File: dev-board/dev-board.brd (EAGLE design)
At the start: 49.2 x 64.8 mm, 44 parts, among them J1 12401832E402A, U1 STM32F103RET6, U2 AT24C64BN-10SU-2.7, U3 FT232RL, U4 MCP2551, U5 Value, X1 8MHz

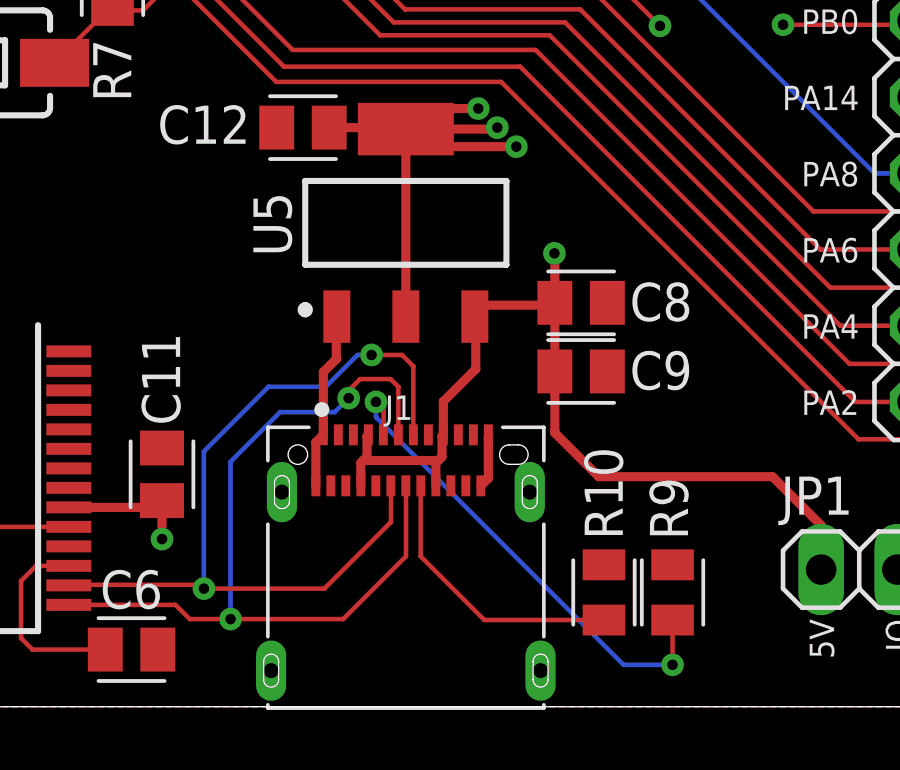
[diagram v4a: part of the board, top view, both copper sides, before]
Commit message: Move R9 to the opposite side of the connector
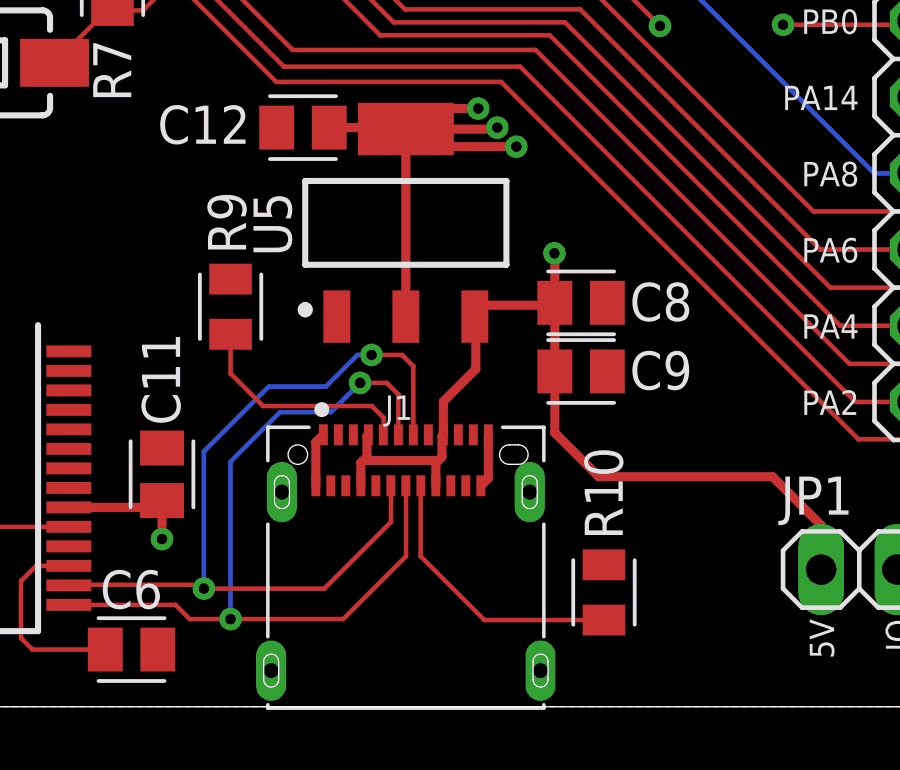
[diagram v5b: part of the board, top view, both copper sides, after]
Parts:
- moved R9 17.5 mm to (16.6, 13.3)
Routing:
- net N$13: track 16.5 -> 7.59 mm, vias 2 -> 0
- net GND: track 7.78 -> 3.66 mm
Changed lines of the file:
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@@
 <attribute name="TYPE" value="" x="55.88" y="69.85" size="1.778" layer="27" rot="R90" display="off"/>
 </element>
-<element name="R9" library="Resistor" library_urn="urn:adsk.eagle:library:16378527" package="RESC2012X65" package3d_urn="urn:adsk.eagle:package:16378559/2" value="5K1" x="31.369" y="3.81" smashed="yes" rot="R270">
-<attribute name="CATEGORY" value="Resistor" x="-21.971" y="-46.99" size="1.778" layer="27" rot="R270" display="off"/>
-<attribute name="MANUFACTURER" value="" x="-21.971" y="-46.99" size="1.778" layer="27" rot="R270" display="off"/>
-<attribute name="MPN" value="" x="-21.971" y="-46.99" size="1.778" layer="27" rot="R270" display="off"/>
-<attribute name="NAME" x="31.8851" y="6.604" size="1.27" layer="25" rot="R90" align="bottom-center"/>
-<attribute name="OPERATING_TEMP" value="" x="-21.971" y="-46.99" size="1.778" layer="27" rot="R270" display="off"/>
-<attribute name="PART_STATUS" value="" x="-21.971" y="-46.99" size="1.778" layer="27" rot="R270" display="off"/>
-<attribute name="RATING" value="" x="-21.971" y="-46.99" size="1.778" layer="27" rot="R270" display="off"/>
-<attribute name="ROHS_COMPLIANT" value="" x="-21.971" y="-46.99" size="1.778" layer="27" rot="R270" display="off"/>
-<attribute name="SERIES" value="" x="-21.971" y="-46.99" size="1.778" layer="27" rot="R270" display="off"/>
-<attribute name="SUB-CATEGORY" value="Fixed" x="-21.971" y="-46.99" size="1.778" layer="27" rot="R270" display="off"/>
-<attribute name="THERMALLOSS" value="" x="-21.971" y="-46.99" size="1.778" layer="27" rot="R270" display="off"/>
-<attribute name="TOLERANCE" value="" x="-21.971" y="-46.99" size="1.778" layer="27" rot="R270" display="off"/>
-<attribute name="TYPE" value="" x="-21.971" y="-46.99" size="1.778" layer="27" rot="R270" display="off"/>
+<element name="R9" library="Resistor" library_urn="urn:adsk.eagle:library:16378527" package="RESC2012X65" package3d_urn="urn:adsk.eagle:package:16378559/2" value="5K1" x="16.637" y="13.335" smashed="yes" rot="R270">
+<attribute name="CATEGORY" value="Resistor" x="-36.703" y="-37.465" size="1.778" layer="27" rot="R270" display="off"/>
+<attribute name="MANUFACTURER" value="" x="-36.703" y="-37.465" size="1.778" layer="27" rot="R270" display="off"/>
+<attribute name="MPN" value="" x="-36.703" y="-37.465" size="1.778" layer="27" rot="R270" display="off"/>
+<attribute name="NAME" x="17.1531" y="16.129" size="1.27" layer="25" rot="R90" align="bottom-center"/>
+<attribute name="OPERATING_TEMP" value="" x="-36.703" y="-37.465" size="1.778" layer="27" rot="R270" display="off"/>
+<attribute name="PART_STATUS" value="" x="-36.703" y="-37.465" size="1.778" layer="27" rot="R270" display="off"/>
+<attribute name="RATING" value="" x="-36.703" y="-37.465" size="1.778" layer="27" rot="R270" display="off"/>
+<attribute name="ROHS_COMPLIANT" value="" x="-36.703" y="-37.465" size="1.778" layer="27" rot="R270" display="off"/>
+<attribute name="SERIES" value="" x="-36.703" y="-37.465" size="1.778" layer="27" rot="R270" display="off"/>
+<attribute name="SUB-CATEGORY" value="Fixed" x="-36.703" y="-37.465" size="1.778" layer="27" rot="R270" display="off"/>
+<attribute name="THERMALLOSS" value="" x="-36.703" y="-37.465" size="1.778" layer="27" rot="R270" display="off"/>
+<attribute name="TOLERANCE" value="" x="-36.703" y="-37.465" size="1.778" layer="27" rot="R270" display="off"/>
+<attribute name="TYPE" value="" x="-36.703" y="-37.465" size="1.778" layer="27" rot="R270" display="off"/>
 </element>
 <element name="S1" library="SparkFun-Switches" library_urn="urn:adsk.eagle:library:535" package="TACTILE_SWITCH_SMD_6.0X3.5MM" package3d_urn="urn:adsk.eagle:package:40165/1" value="NRST" x="7.62" y="21.463" smashed="yes" rot="R180">
@@
 <wire x1="19.479" y1="7.364" x2="19.479" y2="8.814" width="0.3048" layer="1"/>
 <wire x1="19.479" y1="8.814" x2="19.729" y2="9.064" width="0.3048" layer="1"/>
-<wire x1="20.179" y1="11.607" x2="20.161" y2="11.589" width="0.3048" layer="1"/>
-<wire x1="20.161" y1="11.589" x2="19.729" y2="11.157" width="0.3048" layer="1"/>
-<wire x1="19.729" y1="11.157" x2="19.729" y2="9.064" width="0.3048" layer="1"/>
 <contactref element="C10" pad="2"/>
 <contactref element="C11" pad="2"/>
@@
 <contactref element="C8" pad="2"/>
 <contactref element="C9" pad="2"/>
-<wire x1="20.161" y1="11.589" x2="20.161" y2="12.986" width="0.3048" layer="1"/>
 <wire x1="20.161" y1="12.986" x2="20.179" y2="13.004" width="0.3048" layer="1"/>
 <wire x1="24.979" y1="7.364" x2="25.229" y2="7.614" width="0.3048" layer="1"/>
@@
 <contactref element="R9" pad="2"/>
 <contactref element="J1" pad="A5"/>
-<via x="21.4828" y="10.16" extent="1-16" drill="0.35"/>
-<wire x1="21.4828" y1="10.1414875" x2="21.4828" y2="10.16" width="0.1524" layer="1"/>
-<wire x1="21.737" y1="9.8872875" x2="21.737" y2="9.072" width="0.1524" layer="1"/>
 <wire x1="21.729" y1="9.064" x2="21.737" y2="9.072" width="0.1524" layer="1"/>
-<wire x1="21.737" y1="9.8872875" x2="21.4828" y2="10.1414875" width="0.1524" layer="1"/>
-<wire x1="29.7378" y1="1.397" x2="21.4828" y2="9.652" width="0.1524" layer="16"/>
-<wire x1="21.4828" y1="10.16" x2="21.4828" y2="9.652" width="0.1524" layer="16"/>
-<wire x1="29.7378" y1="1.397" x2="31.369" y2="1.397" width="0.1524" layer="16"/>
-<via x="31.369" y="1.397" extent="1-16" drill="0.35"/>
-<wire x1="31.369" y1="1.397" x2="31.369" y2="2.8905" width="0.1524" layer="1"/>
+<wire x1="21.3466875" y1="10.0236" x2="17.7214" y2="10.0236" width="0.1524" layer="1"/>
+<wire x1="16.637" y1="12.4155" x2="16.637" y2="11.108" width="0.1524" layer="1"/>
+<wire x1="17.7214" y1="10.0236" x2="16.637" y2="11.108" width="0.1524" layer="1"/>
+<wire x1="21.737" y1="9.6332875" x2="21.737" y2="9.072" width="0.1524" layer="1"/>
+<wire x1="21.737" y1="9.6332875" x2="21.3466875" y2="10.0236" width="0.1524" layer="1"/>
 </signal>
 <signal name="N$17">
@@
 <contactref element="J1" pad="A6"/>
 <contactref element="J1" pad="B6"/>
-<wire x1="22.229" y1="9.064" x2="22.229" y2="10.664" width="0.1524" layer="1"/>
-<wire x1="22.229" y1="10.664" x2="21.971" y2="10.922" width="0.1524" layer="1"/>
-<wire x1="21.971" y1="10.922" x2="20.955" y2="10.922" width="0.1524" layer="1"/>
-<wire x1="20.955" y1="10.922" x2="20.574" y2="10.541" width="0.1524" layer="1"/>
-<wire x1="20.574" y1="10.541" x2="20.574" y2="10.287" width="0.1524" layer="1"/>
-<via x="20.574" y="10.287" extent="1-16" drill="0.35"/>
+<wire x1="22.229" y1="9.064" x2="22.229" y2="10.41" width="0.1524" layer="1"/>
+<wire x1="22.229" y1="10.41" x2="21.844" y2="10.795" width="0.1524" layer="1"/>
+<wire x1="21.844" y1="10.795" x2="20.955" y2="10.795" width="0.1524" layer="1"/>
+<via x="20.955" y="10.795" extent="1-16" drill="0.35"/>
 <via x="16.637" y="2.921" extent="1-16" drill="0.35"/>
-<wire x1="20.574" y1="10.287" x2="20.1082" y2="9.8212" width="0.1524" layer="16"/>
-<wire x1="20.1082" y1="9.8212" x2="18.291975" y2="9.8212" width="0.1524" layer="16"/>
+<wire x1="20.955" y1="10.795" x2="19.9812" y2="9.8212" width="0.1524" layer="16"/>
+<wire x1="19.9812" y1="9.8212" x2="18.291975" y2="9.8212" width="0.1524" layer="16"/>
 <wire x1="18.291975" y1="9.8212" x2="16.637" y2="8.166225" width="0.1524" layer="16"/>
 <wire x1="16.637" y1="8.166225" x2="16.637" y2="2.921" width="0.1524" layer="16"/>

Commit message: Move 5V trace to the right a bit
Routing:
- net +5V: track 119.1 -> 118.5 mm
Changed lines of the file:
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@@
 <wire x1="17.1316" y1="6.5906" x2="16.129" y2="5.588" width="0.3048" layer="15"/>
 <wire x1="17.1316" y1="6.5906" x2="17.1316" y2="10.0385875" width="0.3048" layer="15"/>
-<wire x1="0.508" y1="4.826" x2="-1.27" y2="6.604" width="0.3048" layer="15"/>
-<wire x1="-1.27" y1="38.354" x2="7.493" y2="47.117" width="0.3048" layer="15"/>
-<wire x1="-1.27" y1="6.604" x2="-1.27" y2="38.354" width="0.3048" layer="15"/>
+<wire x1="0.508" y1="4.826" x2="-0.508" y2="5.842" width="0.3048" layer="15"/>
+<wire x1="-0.508" y1="39.116" x2="7.493" y2="47.117" width="0.3048" layer="15"/>
+<wire x1="-0.508" y1="5.842" x2="-0.508" y2="39.116" width="0.3048" layer="15"/>
 <contactref element="JP1" pad="1"/>
 <wire x1="27.4456" y1="9.1304" x2="28.908" y2="7.668" width="0.3048" layer="1"/>

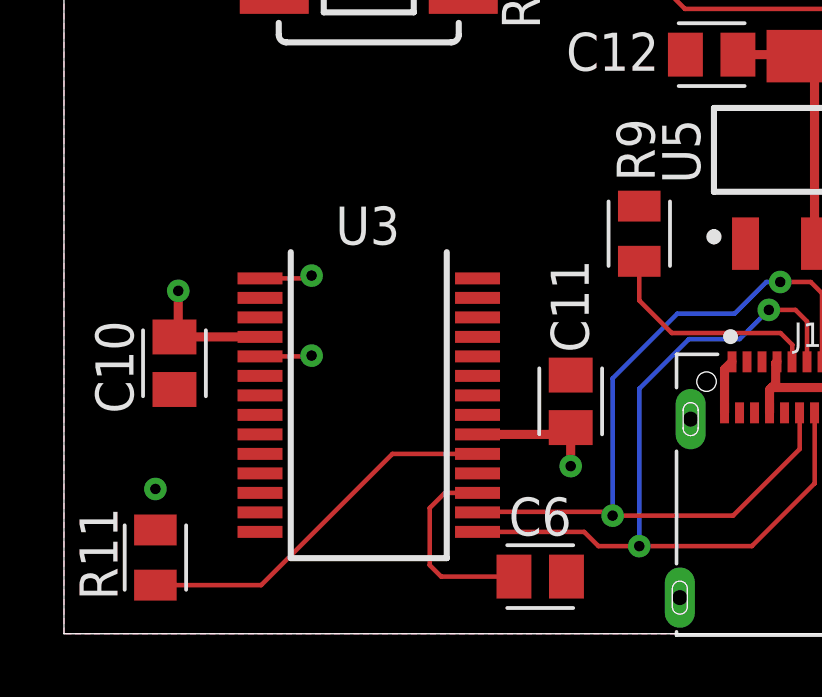
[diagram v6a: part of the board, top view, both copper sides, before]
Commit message: Move C6 closer to the pin
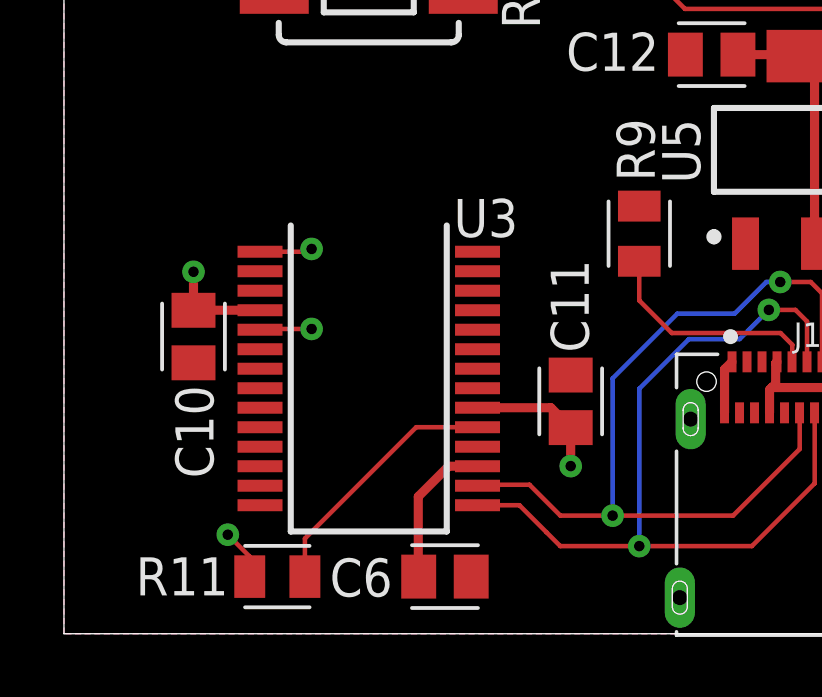
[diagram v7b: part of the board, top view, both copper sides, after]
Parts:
- moved R11 4.11 mm to (4.57, 1.91), turned to 0 degrees
- moved C6 3.18 mm to (10.2, 1.91)
- moved C10 1.09 mm to (1.78, 9.91)
- moved U3 0.89 mm to (7.62, 8.51)
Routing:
- net +5V: track 118.5 -> 122.9 mm
- net N$15: track 12.5 -> 8.56 mm
- net N$10: track 6.67 -> 5.07 mm
- net +3V3: track 67.3 -> 66.3 mm
- net USART_TX: track 54.0 -> 53.2 mm
- net USART_RX: track 54.9 -> 54.3 mm

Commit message: Better ground stitching
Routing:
- net GND: track 3.66 -> 23.6 mm, vias 0 -> 5
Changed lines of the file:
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@@
 <contactref element="C18" pad="2"/>
 <contactref element="C17" pad="2"/>
+<wire x1="19.479" y1="7.364" x2="19.479" y2="6.302" width="0.3048" layer="1"/>
+<wire x1="19.479" y1="6.302" x2="20.066" y2="5.715" width="0.3048" layer="1"/>
+<via x="20.066" y="5.715" extent="1-16" drill="0.35"/>
+<wire x1="20.066" y1="5.715" x2="25.019" y2="5.715" width="0.3048" layer="16"/>
+<via x="25.019" y="5.715" extent="1-16" drill="0.35"/>
+<wire x1="25.019" y1="5.715" x2="26.0045" y2="4.7295" width="0.3048" layer="1"/>
+<wire x1="26.0045" y1="4.7295" x2="29.083" y2="4.7295" width="0.3048" layer="1"/>
+<wire x1="24.979" y1="7.364" x2="24.979" y2="5.755" width="0.3048" layer="1"/>
+<wire x1="24.979" y1="5.755" x2="25.019" y2="5.715" width="0.3048" layer="1"/>
+<wire x1="29.083" y1="4.7295" x2="30.3225" y2="4.7295" width="0.3048" layer="1"/>
+<wire x1="30.3225" y1="4.7295" x2="31.242" y2="3.81" width="0.3048" layer="1"/>
+<via x="31.242" y="3.81" extent="1-16" drill="0.35"/>
+<wire x1="30.3225" y1="4.7295" x2="31.2115" y2="4.7295" width="0.3048" layer="1"/>
+<wire x1="31.2115" y1="4.7295" x2="32.131" y2="3.81" width="0.3048" layer="1"/>
+<via x="32.131" y="3.81" extent="1-16" drill="0.35"/>
+<wire x1="31.2115" y1="4.7295" x2="32.1005" y2="4.7295" width="0.3048" layer="1"/>
+<wire x1="32.1005" y1="4.7295" x2="33.02" y2="3.81" width="0.3048" layer="1"/>
+<via x="33.02" y="3.81" extent="1-16" drill="0.35"/>
+<wire x1="17.855" y1="48.895" x2="21.1954" y2="54.864" width="0" layer="19" extent="1-1"/>
+<wire x1="18.1305" y1="44.45" x2="17.855" y2="48.895" width="0" layer="19" extent="1-1"/>
+<wire x1="18.34" y1="41.31" x2="18.1305" y2="44.45" width="0" layer="19" extent="1-1"/>
+<wire x1="14.732" y1="42.6584" x2="18.1305" y2="44.45" width="0" layer="19" extent="1-1"/>
+<wire x1="13.8566" y1="44.45" x2="14.732" y2="42.6584" width="0" layer="19" extent="1-1"/>
+<wire x1="12.7965" y1="47.879" x2="13.8566" y2="44.45" width="0" layer="19" extent="1-1"/>
+<wire x1="12.7965" y1="50.165" x2="12.7965" y2="47.879" width="0" layer="19" extent="1-1"/>
+<wire x1="12.7965" y1="52.451" x2="12.7965" y2="50.165" width="0" layer="19" extent="1-1"/>
+<wire x1="12.7965" y1="54.737" x2="12.7965" y2="52.451" width="0" layer="19" extent="1-1"/>
+<wire x1="12.954" y1="35.0384" x2="14.732" y2="42.6584" width="0" layer="19" extent="1-1"/>
 <wire x1="15.84" y1="33.81" x2="12.954" y2="35.0384" width="0" layer="19" extent="1-1"/>
+<wire x1="18.34" y1="29.81" x2="15.84" y2="33.81" width="0" layer="19" extent="1-1"/>
 <wire x1="17.907" y1="25.6676" x2="18.34" y2="29.81" width="0" layer="19" extent="1-1"/>
-<wire x1="25.5406" y1="27.305" x2="30.5105" y2="27.305" width="0" layer="19" extent="1-1"/>
+<wire x1="12.954" y1="29.8586" x2="15.84" y2="33.81" width="0" layer="19" extent="1-1"/>
+<wire x1="18.1746" y1="19.304" x2="17.907" y2="25.6676" width="0" layer="19" extent="1-1"/>
+<wire x1="16.637" y1="14.2545" x2="18.1746" y2="19.304" width="0" layer="19" extent="1-1"/>
+<wire x1="20.179" y1="13.004" x2="16.637" y2="14.2545" width="0" layer="19" extent="1-1"/>
+<wire x1="19.729" y1="9.064" x2="20.179" y2="13.004" width="0" layer="19" extent="1-1"/>
+<wire x1="18.349" y1="7.154" x2="19.479" y2="7.364" width="0" layer="19" extent="1-1"/>
+<wire x1="26.609" y1="7.154" x2="24.979" y2="7.364" width="0" layer="19" extent="1-1"/>
+<wire x1="26.969" y1="1.204" x2="29.083" y2="4.7295" width="0" layer="19" extent="1-1"/>
+<wire x1="14.351" y1="8.6224" x2="18.349" y2="7.154" width="0" layer="19" extent="1-1"/>
+<wire x1="11.2632" y1="8.2022" x2="14.351" y2="8.6224" width="0" layer="19" extent="1-1"/>
+<wire x1="11.245" y1="6.234" x2="11.245" y2="8.184" width="0" layer="19" extent="1-1"/>
+<wire x1="11.245" y1="10.784" x2="11.2632" y2="8.2022" width="0" layer="19" extent="1-1"/>
+<wire x1="11.245" y1="11.434" x2="11.245" y2="10.784" width="0" layer="19" extent="1-1"/>
+<wire x1="11.0354" y1="1.905" x2="11.245" y2="6.234" width="0" layer="19" extent="1-1"/>
+<wire x1="29.1964" y1="11.176" x2="25.229" y2="9.064" width="0" layer="19" extent="1-1"/>
+<wire x1="29.1964" y1="13.462" x2="29.1964" y2="11.176" width="0" layer="19" extent="1-1"/>
+<wire x1="17.989" y1="1.204" x2="20.066" y2="5.715" width="0" layer="19" extent="1-1"/>
+<wire x1="24.84" y1="29.81" x2="18.34" y2="29.81" width="0" layer="19" extent="1-1"/>
+<wire x1="25.5406" y1="27.305" x2="24.84" y2="29.81" width="0" layer="19" extent="1-1"/>
+<wire x1="30.5105" y1="27.305" x2="25.5406" y2="27.305" width="0" layer="19" extent="1-1"/>
+<wire x1="30.4664" y1="29.591" x2="30.5105" y2="27.305" width="0" layer="19" extent="1-1"/>
+<wire x1="3.995" y1="8.834" x2="11.245" y2="8.184" width="0" layer="19" extent="1-1"/>
+<wire x1="1.778" y1="9.0306" x2="3.995" y2="8.834" width="0" layer="19" extent="1-1"/>
+<wire x1="5.334" y1="35.5464" x2="12.954" y2="35.0384" width="0" layer="19" extent="1-1"/>
+<wire x1="5.334" y1="37.7326" x2="5.334" y2="35.5464" width="0" layer="19" extent="1-1"/>
+<wire x1="4.445" y1="49.6007" x2="12.7965" y2="50.165" width="0" layer="19" extent="1-1"/>
+<wire x1="4.2046" y1="47.117" x2="4.445" y2="49.6007" width="0" layer="19" extent="1-1"/>
+<wire x1="0.635" y1="51.1505" x2="4.445" y2="49.6007" width="0" layer="19" extent="1-1"/>
+<wire x1="27.34" y1="38.81" x2="18.34" y2="41.31" width="0" layer="19" extent="1-1"/>
+<wire x1="28.956" y1="41.3884" x2="27.34" y2="38.81" width="0" layer="19" extent="1-1"/>
+<wire x1="43.942" y1="4.572" x2="33.02" y2="3.81" width="0" layer="19" extent="1-1"/>
+<wire x1="1.43" y1="62.484" x2="0.635" y2="51.1505" width="0" layer="19" extent="1-1"/>
+<wire x1="4.47" y1="21.463" x2="12.954" y2="29.8586" width="0" layer="19" extent="1-1"/>
+<wire x1="2.54" y1="23.2105" x2="4.47" y2="21.463" width="0" layer="19" extent="1-1"/>
 </signal>
 <signal name="N$13">
